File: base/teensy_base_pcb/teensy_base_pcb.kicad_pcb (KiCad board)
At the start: 2 copper layers, 69.9 x 52.1 mm, 28 parts, among them U1 LM7805CT, U2 LD1117V33, U3 Teensy_3.2, U4 nRF24L01+, U5 TA8428K

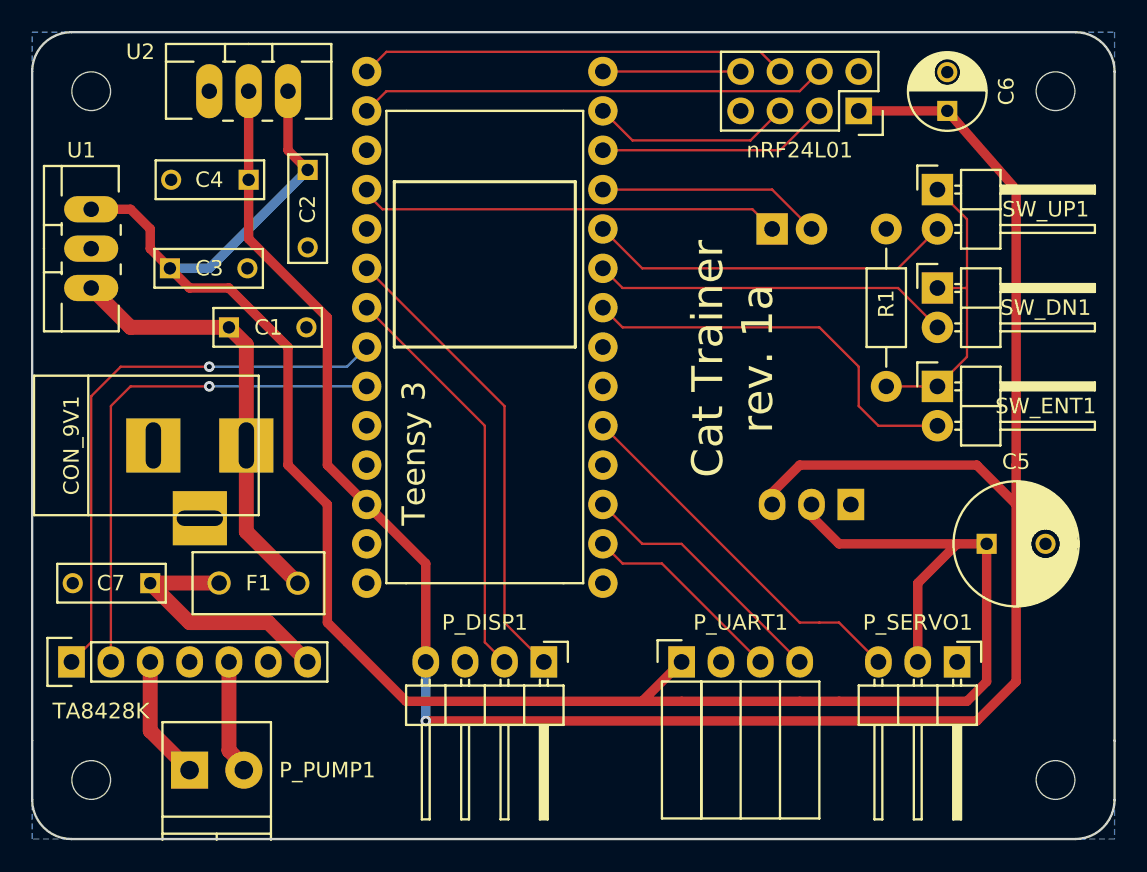
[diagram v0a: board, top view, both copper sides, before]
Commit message: Increase current trace size and clean up labels.
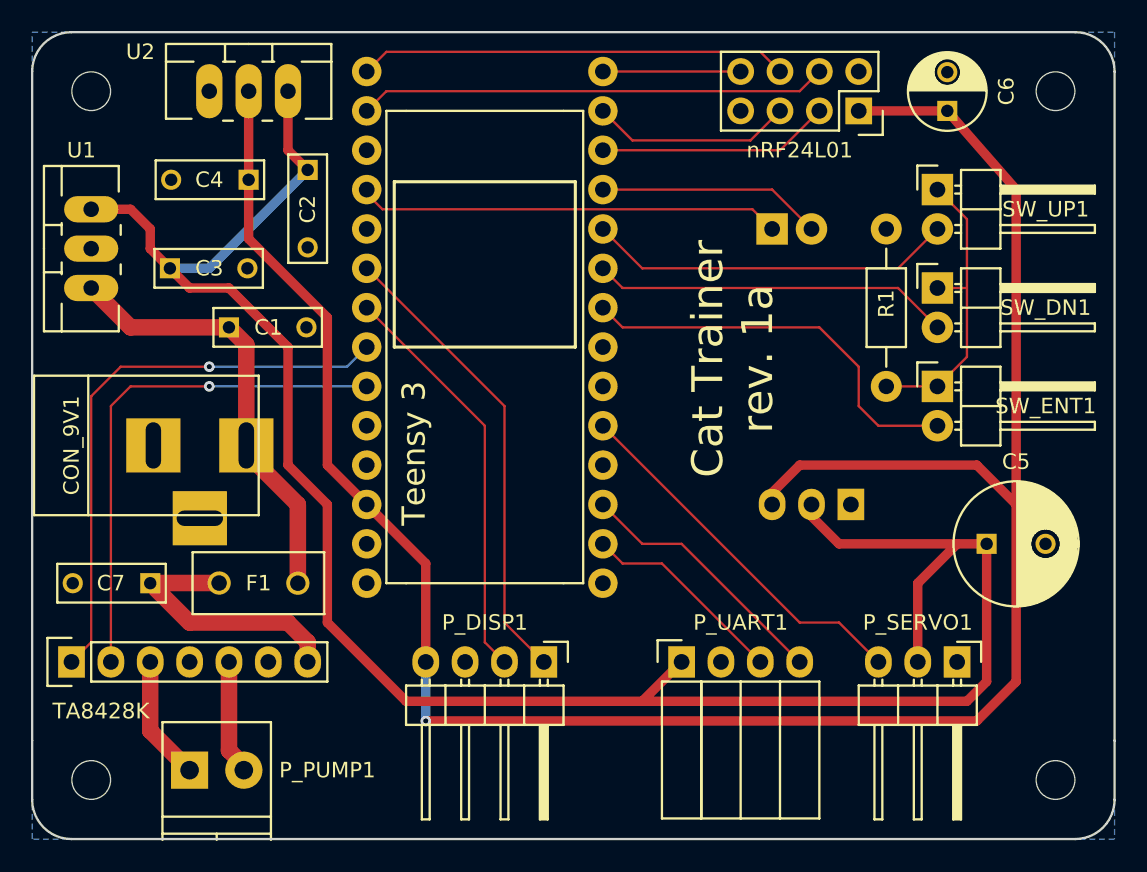
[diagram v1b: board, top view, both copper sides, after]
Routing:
- net Net-(C7-Pad1): track 16.7 -> 17.4 mm
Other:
- net class Current: clearance 0.2032 -> 0.254; trace_width 0.9652 -> 1.0668

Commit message: Move button resistor and more track clean up.
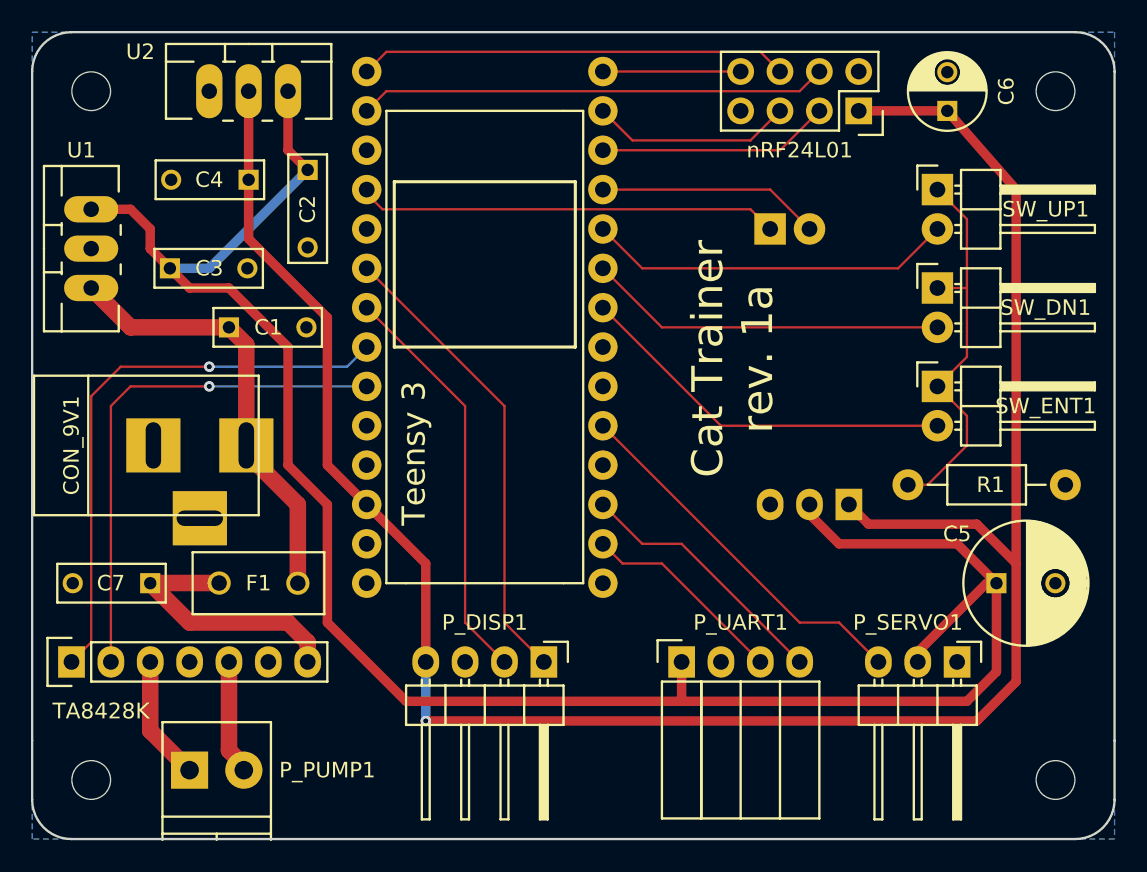
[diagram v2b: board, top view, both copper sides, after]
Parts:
- moved R1 6.50 mm to (159.4, 99.1), turned to 0 degrees
- moved C5 2.62 mm to (165.1, 105.4)
- moved P_ACC1 0.13 mm to (155.6, 100.3)
- moved P_ACC2 0.13 mm to (150.5, 82.5)
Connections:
- P_ACC1 pad 1: GND -> +3.3V
- P_ACC1 pad 3: +3.3V -> GND
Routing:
- net +3.3V: track 147.8 -> 142.0 mm
- net Net-(R1-Pad1): track 20.0 -> 25.6 mm
- net +5V: track 133.5 -> 130.8 mm
- net Net-(SW_ENT1-Pad2): track 26.2 -> 24.7 mm

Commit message: More trace cleanup.
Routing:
- net Net-(R1-Pad1): track 25.6 -> 27.5 mm
- net +5V: track 130.8 -> 132.1 mm
- net +9V: track 28.4 -> 27.8 mm
- net Net-(P_PUMP1-Pad2): track 7.69 -> 7.07 mm
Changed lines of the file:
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@@
     (links 67)
     (no_connects 9)
-    (area 102.794999 69.774999 172.795001 121.995001)
+    (area 94.687429 69.131 192.305715 135.415001)
     (thickness 1.6)
     (drawings 28)
-    (tracks 129)
+    (tracks 121)
     (zones 0)
     (modules 28)
@@
   (segment (start 130.81 107.95) (end 130.81 93.98) (width 0.1524) (layer F.Cu) (net 10))
   (segment (start 130.81 93.98) (end 124.46 87.63) (width 0.1524) (layer F.Cu) (net 10) (status 20))
-  (segment (start 116.69014 96.52) (end 116.69014 97.00514) (width 0.9652) (layer F.Cu) (net 12) (status 30))
   (segment (start 116.69014 97.00514) (end 120.015 100.33) (width 1.0668) (layer F.Cu) (net 12) (status 10))
   (segment (start 120.015 100.33) (end 120.015 105.41) (width 1.0668) (layer F.Cu) (net 12) (status 20))
-  (segment (start 116.69014 96.52) (end 116.84 96.52) (width 0.6096) (layer F.Cu) (net 12) (status 30))
   (segment (start 116.69014 96.52) (end 116.69014 90.02014) (width 1.0668) (layer F.Cu) (net 12) (status 10))
   (segment (start 116.69014 90.02014) (end 115.57 88.9) (width 1.0668) (layer F.Cu) (net 12) (status 20))
   (segment (start 115.57 88.9) (end 109.22 88.9) (width 1.0668) (layer F.Cu) (net 12) (status 10))
   (segment (start 109.22 88.9) (end 106.68 86.36) (width 1.0668) (layer F.Cu) (net 12) (status 20))
-  (segment (start 165.1 105.41) (end 164.465 105.41) (width 0.6096) (layer F.Cu) (net 13) (status 30))
-  (segment (start 164.465 105.41) (end 160.02 109.855) (width 0.6096) (layer F.Cu) (net 13) (status 30))
-  (segment (start 160.02 109.855) (end 160.02 110.49) (width 0.6096) (layer F.Cu) (net 13) (status 30))
+  (segment (start 160.02 106.68) (end 160.02 110.49) (width 0.6096) (layer F.Cu) (net 13))
+  (segment (start 165.1 105.41) (end 161.29 105.41) (width 0.6096) (layer F.Cu) (net 13))
+  (segment (start 161.29 105.41) (end 160.02 106.68) (width 0.6096) (layer F.Cu) (net 13))
+  (segment (start 106.68 81.28) (end 110.49 81.28) (width 0.6096) (layer F.Cu) (net 13))
+  (segment (start 111.76 82.55) (end 111.76 85.09) (width 0.6096) (layer F.Cu) (net 13))
+  (segment (start 110.49 81.28) (end 111.76 82.55) (width 0.6096) (layer F.Cu) (net 13))
   (segment (start 165.1 105.41) (end 162.56 102.87) (width 0.6096) (layer F.Cu) (net 13) (status 10))
+  (segment (start 162.56 102.87) (end 154.94 102.87) (width 0.6096) (layer F.Cu) (net 13))
   (segment (start 154.94 102.87) (end 153.035 100.965) (width 0.6096) (layer F.Cu) (net 13) (status 20))
-  (segment (start 162.56 102.87) (end 154.94 102.87) (width 0.6096) (layer F.Cu) (net 13))
   (segment (start 153.035 100.965) (end 153.035 100.33) (width 0.6096) (layer F.Cu) (net 13) (status 30))
   (segment (start 144.78 110.49) (end 144.78 113.03) (width 0.6096) (layer F.Cu) (net 13) (status 10))
   (segment (start 165.1 105.41) (end 165.1 111.125) (width 0.6096) (layer F.Cu) (net 13) (status 10))
+  (segment (start 165.1 111.125) (end 163.195 113.03) (width 0.6096) (layer F.Cu) (net 13))
   (segment (start 163.195 113.03) (end 144.78 113.03) (width 0.6096) (layer F.Cu) (net 13))
   (segment (start 144.78 113.03) (end 127 113.03) (width 0.6096) (layer F.Cu) (net 13))
-  (segment (start 165.1 111.125) (end 163.195 113.03) (width 0.6096) (layer F.Cu) (net 13))
-  (segment (start 110.49 82.55) (end 109.22 81.28) (width 0.6096) (layer F.Cu) (net 13))
-  (segment (start 110.49 83.82) (end 110.49 82.55) (width 0.6096) (layer F.Cu) (net 13))
-  (segment (start 109.22 81.28) (end 106.68 81.28) (width 0.6096) (layer F.Cu) (net 13) (status 20))
-  (segment (start 111.76 85.09) (end 110.49 83.82) (width 0.6096) (layer F.Cu) (net 13) (status 10))
   (segment (start 121.92 107.95) (end 127 113.03) (width 0.6096) (layer F.Cu) (net 13))
   (segment (start 113.03 86.36) (end 115.57 86.36) (width 0.6096) (layer F.Cu) (net 13))
@@
   (segment (start 111.76 85.09) (end 114.3 85.09) (width 0.6096) (layer B.Cu) (net 13) (status 10))
   (segment (start 114.3 85.09) (end 120.65 78.74) (width 0.6096) (layer B.Cu) (net 13) (status 20))
-  (segment (start 106.68 81.28) (end 107.95 81.28) (width 0.6096) (layer F.Cu) (net 13) (status 30))
   (segment (start 120.65 78.74) (end 119.38 77.47) (width 0.6096) (layer F.Cu) (net 13) (status 10))
   (segment (start 119.38 77.47) (end 119.38 73.66) (width 0.6096) (layer F.Cu) (net 13) (status 20))
@@
   (segment (start 156.845 101.6) (end 155.575 100.33) (width 0.6096) (layer F.Cu) (net 14) (status 20))
   (segment (start 163.83 101.6) (end 156.845 101.6) (width 0.6096) (layer F.Cu) (net 14))
-  (segment (start 155.575 100.33) (end 155.575 100.457) (width 0.6096) (layer F.Cu) (net 14) (status 30))
   (segment (start 124.46 100.33) (end 128.27 104.14) (width 0.6096) (layer F.Cu) (net 14) (status 10))
   (segment (start 128.27 104.14) (end 128.27 110.49) (width 0.6096) (layer F.Cu) (net 14) (status 20))
@@
   (segment (start 158.75 85.09) (end 161.29 82.55) (width 0.1524) (layer F.Cu) (net 17) (status 20))
   (segment (start 142.24 85.09) (end 158.75 85.09) (width 0.1524) (layer F.Cu) (net 17))
+  (segment (start 163.195 88.265) (end 163.195 94.615) (width 0.1524) (layer F.Cu) (net 18))
+  (segment (start 161.29 86.36) (end 163.195 88.265) (width 0.1524) (layer F.Cu) (net 18) (status 10))
   (segment (start 163.195 94.615) (end 163.195 96.52) (width 0.1524) (layer F.Cu) (net 18))
+  (segment (start 163.195 96.52) (end 160.655 99.06) (width 0.1524) (layer F.Cu) (net 18))
+  (segment (start 160.655 99.06) (end 159.385 99.06) (width 0.1524) (layer F.Cu) (net 18) (status 20))
   (segment (start 161.29 92.71) (end 163.195 94.615) (width 0.1524) (layer F.Cu) (net 18) (status 10))
-  (segment (start 160.655 99.06) (end 159.385 99.06) (width 0.1524) (layer F.Cu) (net 18) (status 20))
-  (segment (start 163.195 96.52) (end 160.655 99.06) (width 0.1524) (layer F.Cu) (net 18))
-  (segment (start 161.29 86.36) (end 163.195 86.36) (width 0.1524) (layer F.Cu) (net 18) (status 10))
   (segment (start 161.29 80.01) (end 163.195 81.915) (width 0.1524) (layer F.Cu) (net 18) (status 10))
-  (segment (start 163.195 90.805) (end 161.29 92.71) (width 0.1524) (layer F.Cu) (net 18) (status 20))
-  (segment (start 163.195 81.915) (end 163.195 86.36) (width 0.1524) (layer F.Cu) (net 18))
-  (segment (start 163.195 86.36) (end 163.195 90.805) (width 0.1524) (layer F.Cu) (net 18))
+  (segment (start 163.195 81.915) (end 163.195 88.265) (width 0.1524) (layer F.Cu) (net 18))
   (segment (start 150.495 82.55) (end 149.225 81.28) (width 0.1524) (layer F.Cu) (net 19) (status 10))
   (segment (start 124.46 80.01) (end 124.46 80.264) (width 0.1524) (layer F.Cu) (net 19) (status 30))
@@
   (segment (start 115.57 110.49) (end 115.57 116.205) (width 1.0668) (layer F.Cu) (net 21) (status 10))
   (segment (start 115.57 116.205) (end 116.53 117.165) (width 1.0668) (layer F.Cu) (net 21) (status 20))
-  (segment (start 116.53 117.165) (end 116.53 117.475) (width 0.6096) (layer F.Cu) (net 21) (status 30))
-  (segment (start 116.53 117.475) (end 116.53 117.165) (width 0.1524) (layer F.Cu) (net 21) (status 30))
   (segment (start 110.49 110.49) (end 110.49 114.935) (width 1.0668) (layer F.Cu) (net 22) (status 10))
   (segment (start 110.49 114.935) (end 113.03 117.475) (width 1.0668) (layer F.Cu) (net 22) (status 20))

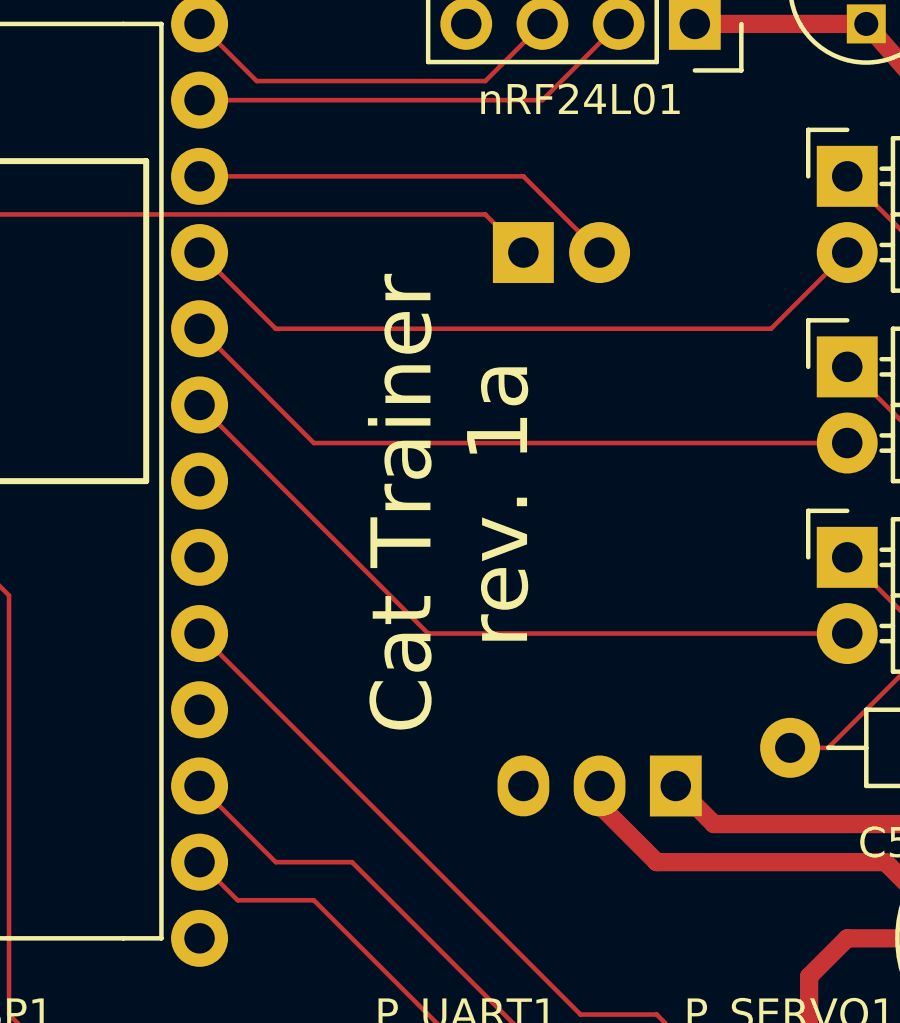
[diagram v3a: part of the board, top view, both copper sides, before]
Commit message: Add document title / rev and set button R value.
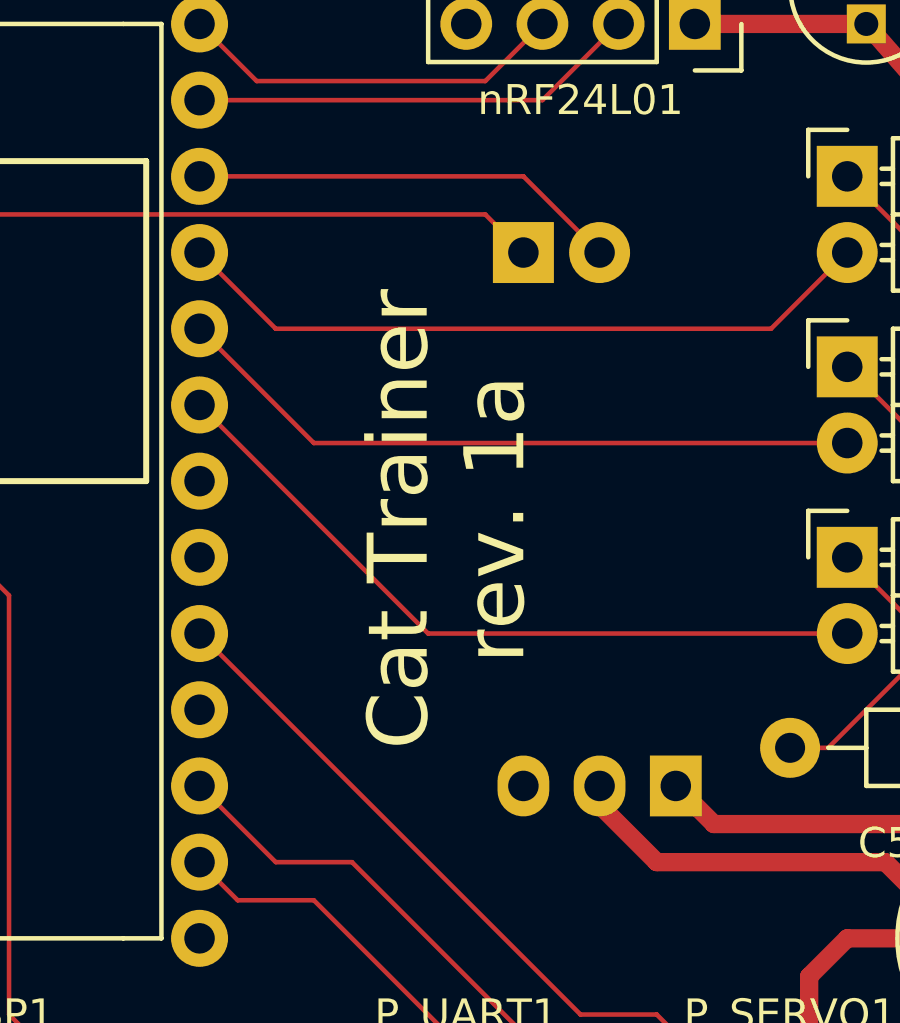
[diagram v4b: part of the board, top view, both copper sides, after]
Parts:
- R1: value 10K -> 100
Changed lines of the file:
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@@
     (links 67)
     (no_connects 9)
-    (area 94.687429 69.131 192.305715 135.415001)
+    (area 102.794999 69.774999 172.795001 121.995001)
     (thickness 1.6)
     (drawings 28)
@@
   )
   (page A4)
+  (title_block
+    (title "Teensy Base PCB")
+    (rev 1a)
+  )
   (layers
     (0 F.Cu signal)
@@
       (effects (font (size 1 1) (thickness 0.15)))
     )
-    (fp_text value 10K (at 5.08 -2.413) (layer F.Fab)
+    (fp_text value 100 (at 5.08 -2.413) (layer F.Fab)
       (effects (font (size 1 1) (thickness 0.15)))
     )
@@
     (effects (font (size 0.635 0.635) (thickness 0.127)) (justify mirror))
   )
-  (gr_text "Cat Trainer\nrev. 1a" (at 148.082 90.932 90) (layer B.SilkS)
+  (gr_text "Cat Trainer\nrev. 1a" (at 147.955 91.44 90) (layer B.SilkS)
     (effects (font (size 2 2) (thickness 0.3)) (justify mirror))
   )
-  (gr_text "Cat Trainer\nrev. 1a" (at 148.082 90.932 90) (layer F.SilkS)
+  (gr_text "Cat Trainer\nrev. 1a" (at 147.955 91.44 90) (layer F.SilkS)
     (effects (font (size 2 2) (thickness 0.3)))
   )
